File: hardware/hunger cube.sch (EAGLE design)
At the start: 39 parts, among them IC1 AVR-MEGA8-PPTH, IC2 LDO 5v, Q1 16Mhz, T1 light, T2 PT204

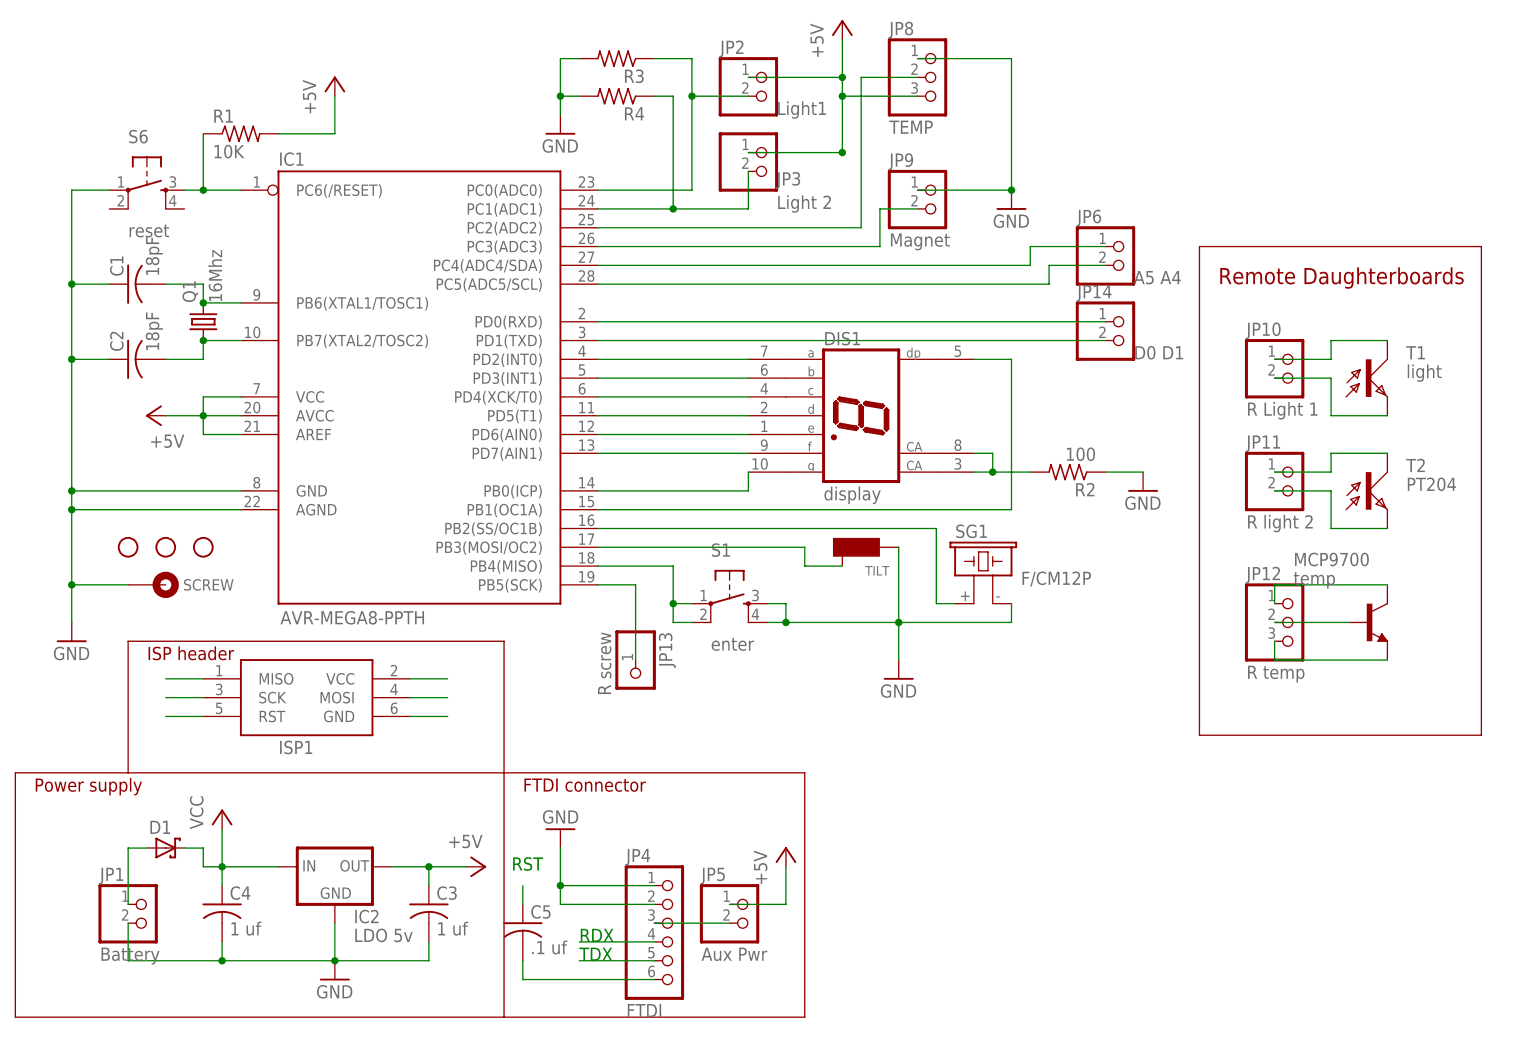
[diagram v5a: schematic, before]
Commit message: 
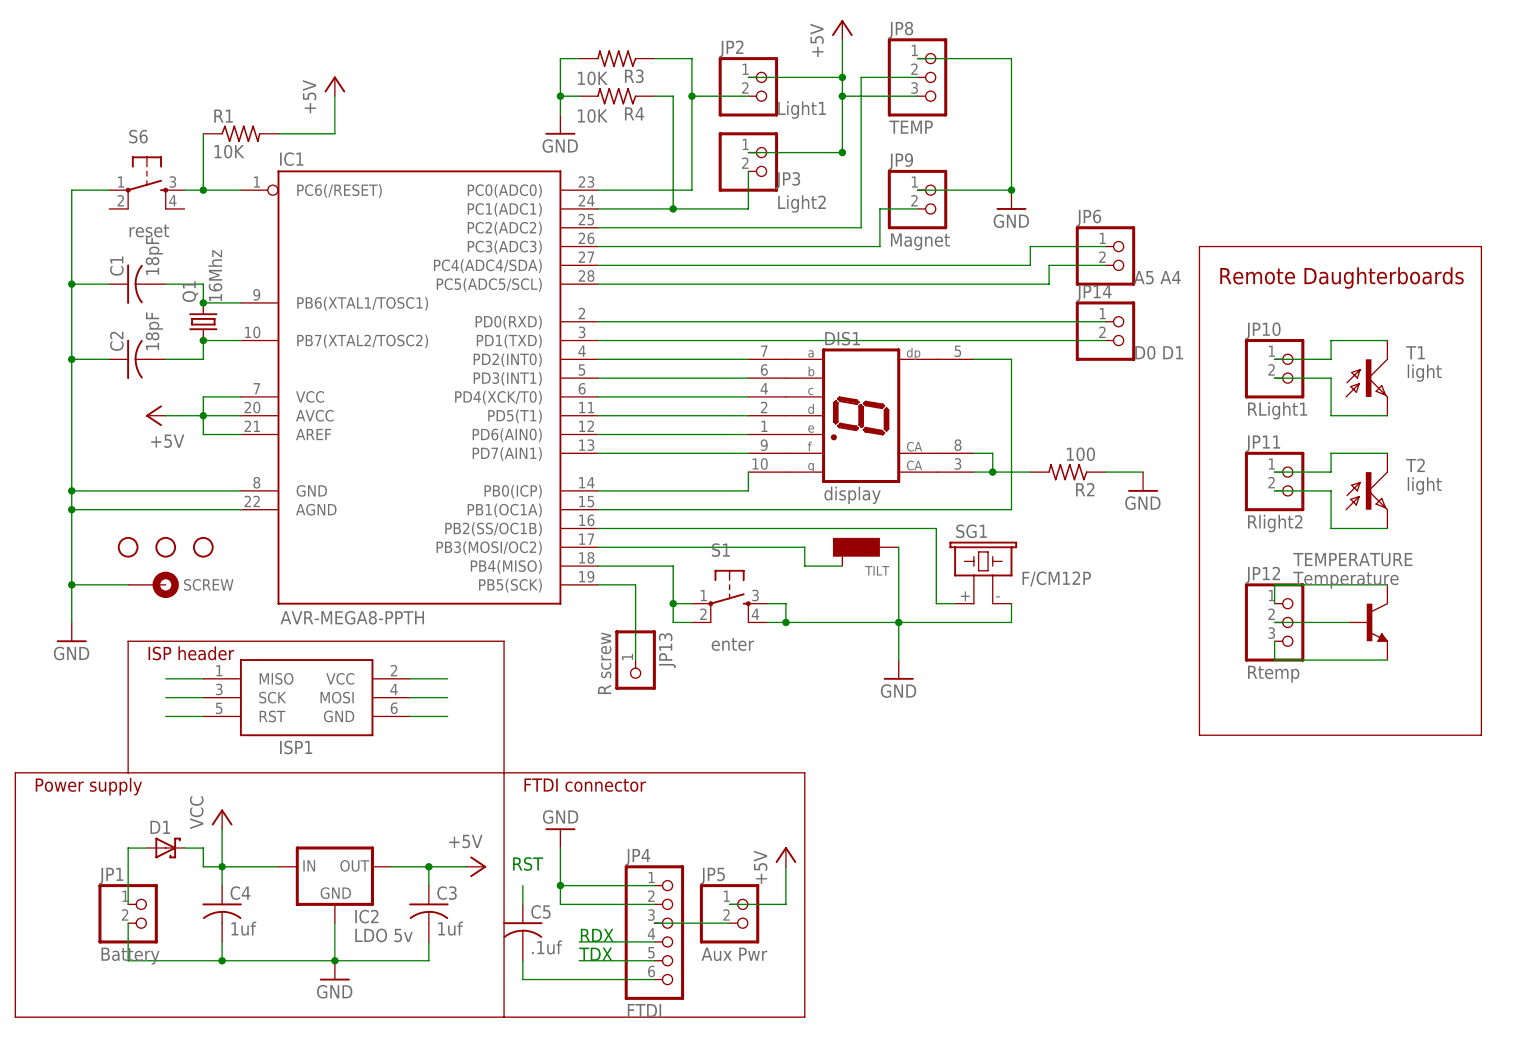
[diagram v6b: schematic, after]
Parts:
- C3, C4: value 1 uf -> 1uf
- C5: value .1 uf -> .1uf
- JP10: value R Light 1 -> RLight1
- JP11: value R light 2 -> Rlight2
- JP12: value R temp -> Rtemp
- JP3: value Light 2 -> Light2
- R3, R4: value (none) -> 10K
- T2: value PT204 -> light
- TEMPERATURE: value temp -> Temperature
- renumbered MCP9700 to TEMPERATURE
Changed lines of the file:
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@@
 <part name="DIS1" library="display-hp" deviceset="HD-H101" device="" value="display"/>
 <part name="IC2" library="adafruit" deviceset="MCP1700" device="INLINE" value="LDO 5v"/>
-<part name="C3" library="resistor" deviceset="C-US" device="025-050X050" value="1 uf"/>
-<part name="C4" library="resistor" deviceset="C-US" device="025-050X050" value="1 uf"/>
+<part name="C3" library="resistor" deviceset="C-US" device="025-050X050" value="1uf"/>
+<part name="C4" library="resistor" deviceset="C-US" device="025-050X050" value="1uf"/>
 <part name="R2" library="resistor" deviceset="R-US_" device="0207/12" value="100"/>
-<part name="R3" library="resistor" deviceset="R-US_" device="0207/12"/>
+<part name="R3" library="resistor" deviceset="R-US_" device="0207/12" value="10K"/>
 <part name="P+1" library="supply1" deviceset="VCC" device=""/>
 <part name="FRAME1" library="frames" deviceset="DOCFIELD" device="" value="1"/>
@@
 <part name="GND4" library="supply1" deviceset="GND" device=""/>
 <part name="JP2" library="pinhead" deviceset="PINHD-1X2" device="" value="Light1"/>
-<part name="JP3" library="pinhead" deviceset="PINHD-1X2" device="" value="Light 2"/>
+<part name="JP3" library="pinhead" deviceset="PINHD-1X2" device="" value="Light2"/>
 <part name="JP8" library="pinhead" deviceset="PINHD-1X3" device="" value="TEMP"/>
-<part name="R4" library="resistor" deviceset="R-US_" device="0207/12"/>
+<part name="R4" library="resistor" deviceset="R-US_" device="0207/12" value="10K"/>
 <part name="GND5" library="supply1" deviceset="GND" device=""/>
 <part name="P+6" library="supply1" deviceset="+5V" device=""/>
-<part name="JP10" library="pinhead" deviceset="PINHD-1X2" device="" value="R Light 1"/>
-<part name="JP11" library="pinhead" deviceset="PINHD-1X2" device="" value="R light 2"/>
+<part name="JP10" library="pinhead" deviceset="PINHD-1X2" device="" value="RLight1"/>
+<part name="JP11" library="pinhead" deviceset="PINHD-1X2" device="" value="Rlight2"/>
 <part name="T1" library="opto-trans-siemens" deviceset="BPX81" device="" value="light"/>
-<part name="T2" library="opto-trans-siemens" deviceset="BPX81" device="" value="PT204"/>
-<part name="MCP9700" library="transistor" deviceset="*-NPN-" device="TO92-EBC" value="temp"/>
-<part name="JP12" library="pinhead" deviceset="PINHD-1X3" device="" value="R temp"/>
+<part name="T2" library="opto-trans-siemens" deviceset="BPX81" device="" value="light"/>
+<part name="TEMPERATURE" library="transistor" deviceset="*-NPN-" device="TO92-EBC" value="Temperature"/>
+<part name="JP12" library="pinhead" deviceset="PINHD-1X3" device="" value="Rtemp"/>
 <part name="GND6" library="supply1" deviceset="GND" device=""/>
 <part name="GND7" library="supply1" deviceset="GND" device=""/>
@@
 <part name="JP6" library="pinhead" deviceset="PINHD-1X2" device="" value="A5 A4"/>
 <part name="JP14" library="pinhead" deviceset="PINHD-1X2" device="" value="D0 D1"/>
-<part name="C5" library="resistor" deviceset="C-US" device="025-050X050" value=".1 uf"/>
+<part name="C5" library="resistor" deviceset="C-US" device="025-050X050" value=".1uf"/>
 <part name="D1" library="adafruit" deviceset="SCHOTTKY-DIODE" device="DO41"/>
 </parts>
@@
 <instance part="C4" gate="G$1" x="-5.08" y="-40.64"/>
 <instance part="R2" gate="G$1" x="109.22" y="17.78" rot="R180"/>
-<instance part="R3" gate="G$1" x="48.26" y="73.66" rot="R180"/>
+<instance part="R3" gate="G$1" x="48.26" y="73.66" smashed="yes" rot="R180">
+<attribute name="NAME" x="52.07" y="72.1614" size="1.778" layer="95" rot="R180"/>
+<attribute name="VALUE" x="46.99" y="71.882" size="1.778" layer="96" rot="R180"/>
+</instance>
 <instance part="P+1" gate="VCC" x="-5.08" y="-27.94"/>
 <instance part="FRAME1" gate="G$1" x="76.2" y="-55.88"/>
@@
 </instance>
 <instance part="JP8" gate="A" x="91.44" y="71.12"/>
-<instance part="R4" gate="G$1" x="48.26" y="68.58" rot="R180"/>
+<instance part="R4" gate="G$1" x="48.26" y="68.58" smashed="yes" rot="R180">
+<attribute name="NAME" x="52.07" y="67.0814" size="1.778" layer="95" rot="R180"/>
+<attribute name="VALUE" x="46.99" y="66.802" size="1.778" layer="96" rot="R180"/>
+</instance>
 <instance part="GND5" gate="1" x="40.64" y="63.5"/>
 <instance part="P+6" gate="1" x="78.74" y="78.74"/>
@@
 <instance part="T1" gate="1" x="149.86" y="30.48"/>
 <instance part="T2" gate="1" x="149.86" y="15.24"/>
-<instance part="MCP9700" gate="G$1" x="149.86" y="-2.54"/>
+<instance part="TEMPERATURE" gate="G$1" x="149.86" y="-2.54"/>
 <instance part="JP12" gate="A" x="139.7" y="-2.54"/>
 <instance part="GND6" gate="1" x="101.6" y="53.34"/>
@@
 <net name="N$20" class="0">
 <segment>
-<pinref part="MCP9700" gate="G$1" pin="E"/>
+<pinref part="TEMPERATURE" gate="G$1" pin="E"/>
 <pinref part="JP12" gate="A" pin="3"/>
 <wire x1="152.4" y1="-7.62" x2="137.16" y2="-7.62" width="0.1524" layer="91"/>
@@
 <net name="N$21" class="0">
 <segment>
-<pinref part="MCP9700" gate="G$1" pin="B"/>
+<pinref part="TEMPERATURE" gate="G$1" pin="B"/>
 <pinref part="JP12" gate="A" pin="2"/>
 <wire x1="147.32" y1="-2.54" x2="137.16" y2="-2.54" width="0.1524" layer="91"/>
@@
 <net name="N$22" class="0">
 <segment>
-<pinref part="MCP9700" gate="G$1" pin="C"/>
+<pinref part="TEMPERATURE" gate="G$1" pin="C"/>
 <pinref part="JP12" gate="A" pin="1"/>
 <wire x1="152.4" y1="2.54" x2="137.16" y2="2.54" width="0.1524" layer="91"/>
